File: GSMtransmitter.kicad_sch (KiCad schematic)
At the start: 44 parts, among them J1 Conn_01x06_Pin, J2 Conn_02x02_2.54, J3 Conn_01x05, SW1 SM5-180UP-1, U1 STM32L052C8Tx, Y1 4 MHz, Y2 32768 kHz

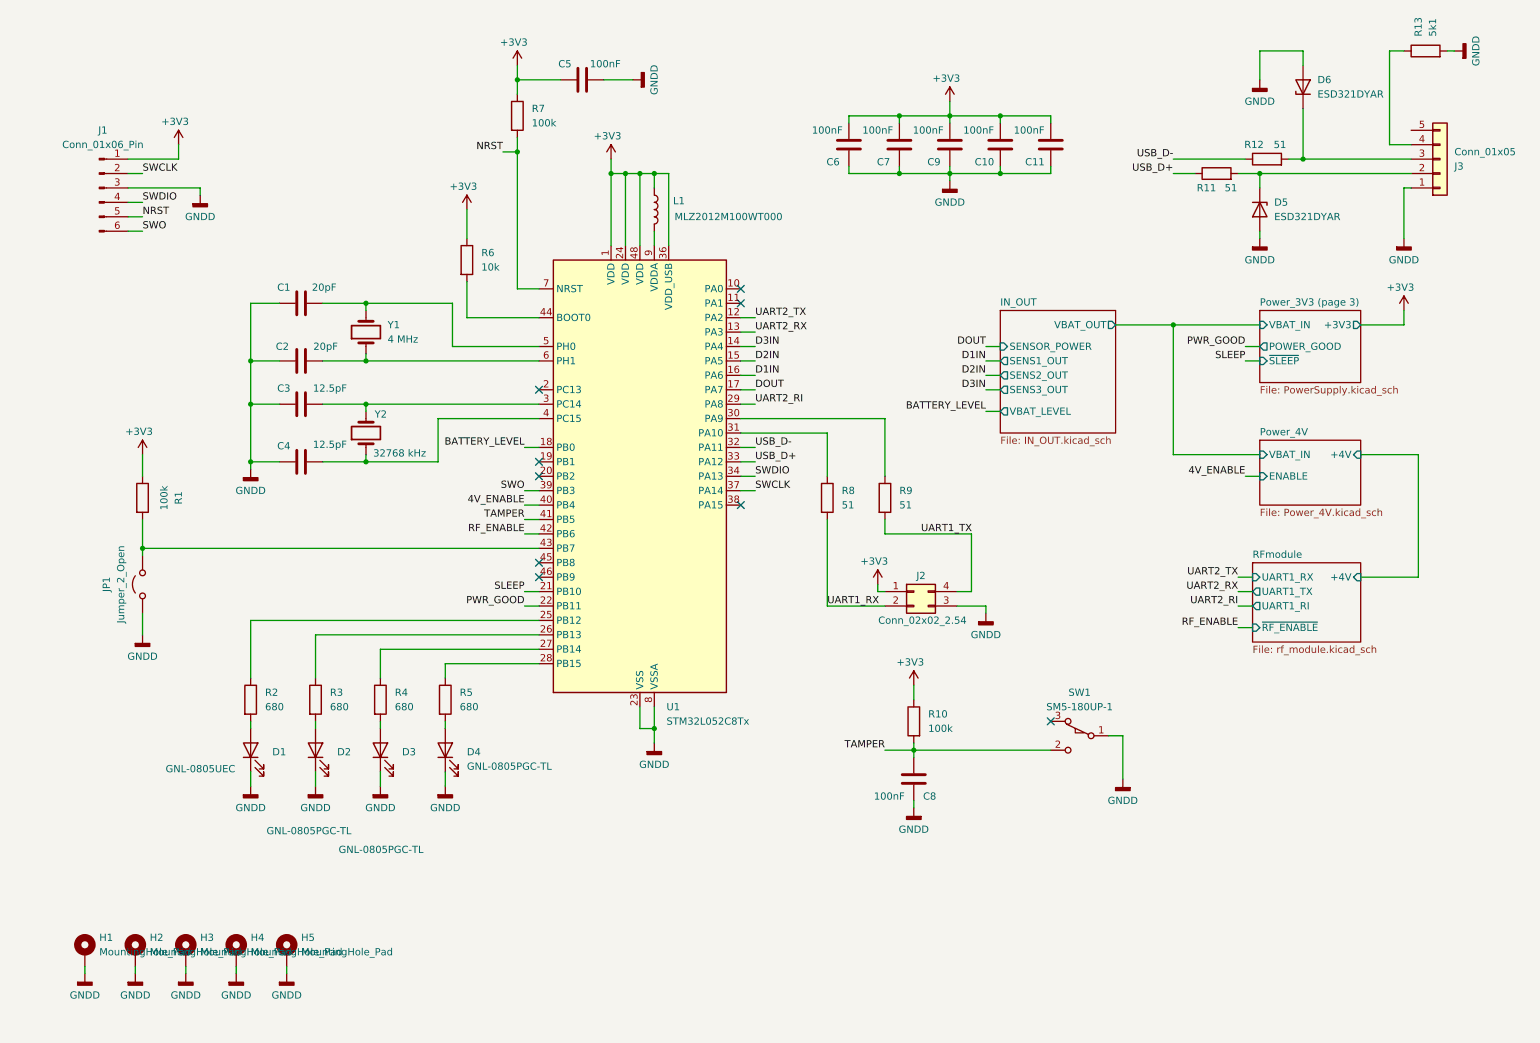
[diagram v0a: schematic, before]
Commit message: Dual SIM version
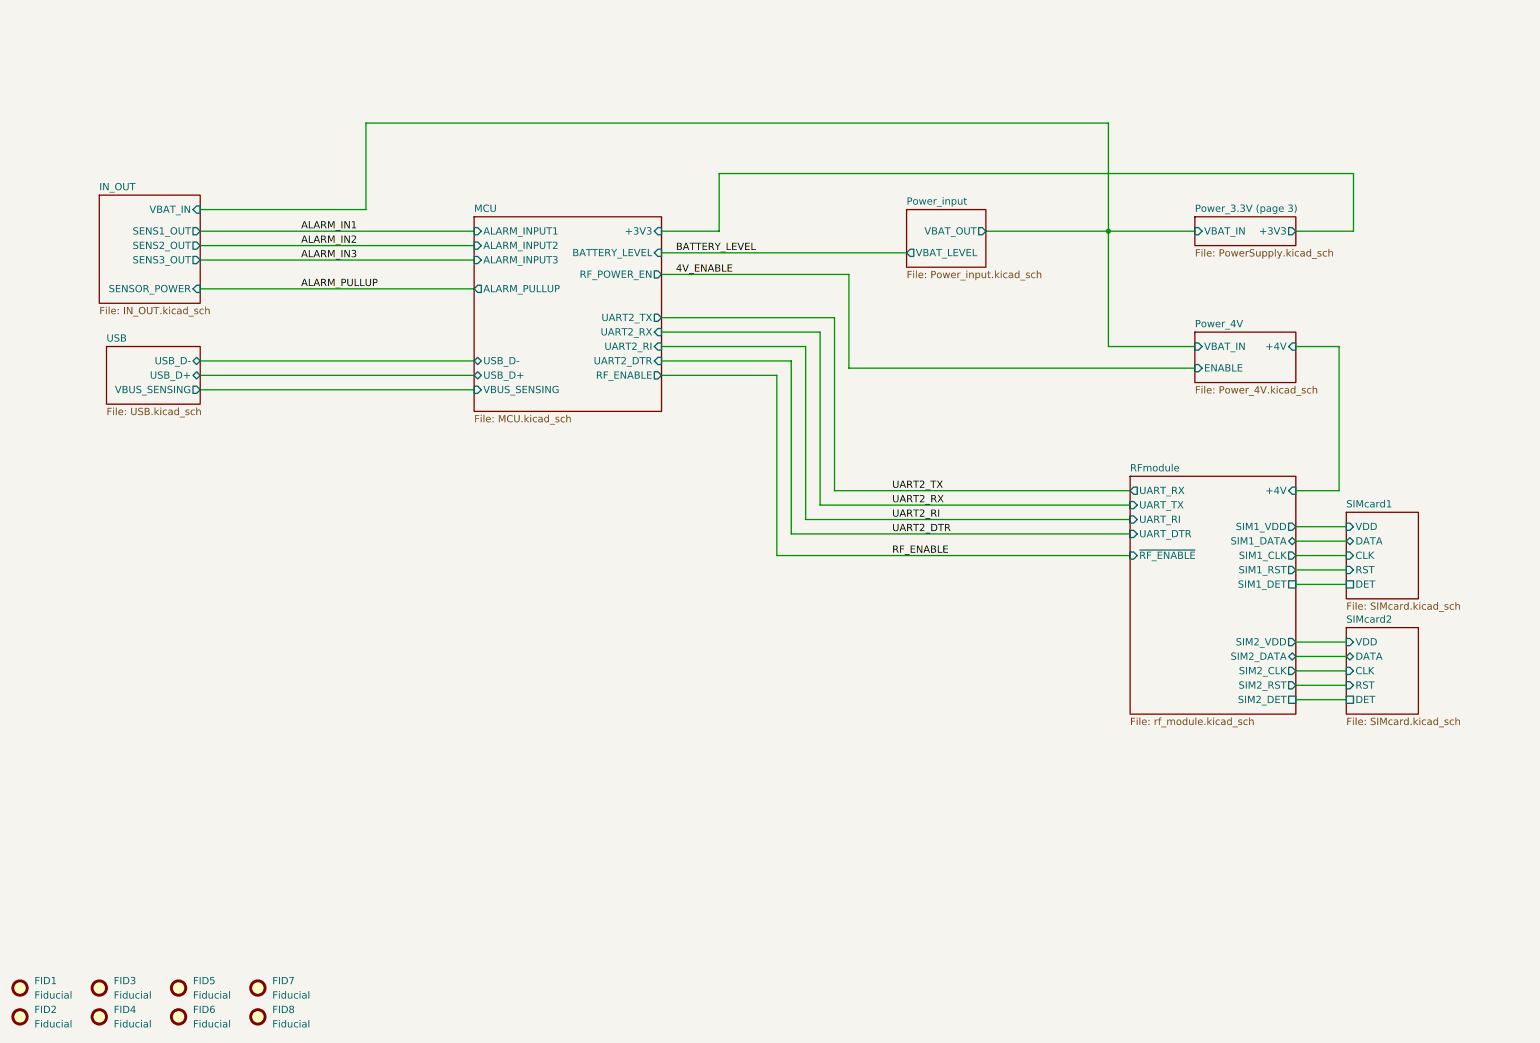
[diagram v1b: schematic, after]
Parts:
- removed C1, C2: 20pF, Capacitor_SMD:C_0805_2012Metric_Pad1.18x1.45mm_HandSolder, symbol Device:C
- removed C10, C11, C5, C6, C7, C8, C9: 100nF, Capacitor_SMD:C_0805_2012Metric_Pad1.18x1.45mm_HandSolder, symbol Device:C
- removed C3, C4: 12.5pF, Capacitor_SMD:C_0805_2012Metric_Pad1.18x1.45mm_HandSolder, symbol Device:C
- removed D1: GNL-0805UEC, LED_SMD:LED_0805_2012Metric_Pad1.15x1.40mm_HandSolder, symbol Device:LED
- removed D2, D3, D4: GNL-0805PGC-TL, LED_SMD:LED_0805_2012Metric_Pad1.15x1.40mm_HandSolder, symbol Device:LED
- removed D5, D6: ESD321DYAR, Diode_SMD:D_SOD-523, symbol Diode:ESD5Zxx
- removed H1, H2, H3, H4: MountingHole_Pad, MountingHole:MountingHole_4.3mm_M4_DIN965_Pad, symbol Mechanical:MountingHole_Pad
- removed H5: MountingHole_Pad, MountingHole:MountingHole_3.5mm_Pad_TopBottom, symbol Mechanical:MountingHole_Pad
- removed J1: Conn_01x06_Pin, Connector_PinHeader_2.54mm:PinHeader_1x06_P2.54mm_Vertical, symbol Connector:Conn_01x06_Pin
- removed J2: Conn_02x02_2.54, Connector_PinSocket_2.54mm:PinSocket_2x02_P2.54mm_Vertical, symbol Connector_Generic:Conn_02x02_Counter_Clockwise
- removed J3: Conn_01x05, Connector_JST:JST_PH_B5B-PH-K_1x05_P2.00mm_Vertical, symbol Connector_Generic:Conn_01x05
- removed JP1: Jumper_2_Open, TestPoint:TestPoint_2Pads_Pitch2.54mm_Drill0.8mm, symbol Jumper:Jumper_2_Open
- removed L1: MLZ2012M100WT000, Inductor_SMD:L_0805_2012Metric_Pad1.05x1.20mm_HandSolder, symbol Device:L
- removed R1, R10, R7: 100k, Resistor_SMD:R_0805_2012Metric_Pad1.20x1.40mm_HandSolder, symbol Device:R
- removed R11, R12, R8, R9: 51, Resistor_SMD:R_0805_2012Metric_Pad1.20x1.40mm_HandSolder, symbol Device:R
- removed R13: 5k1, Resistor_SMD:R_0805_2012Metric_Pad1.20x1.40mm_HandSolder, symbol Device:R
- removed R2, R3, R4, R5: 680, Resistor_SMD:R_0805_2012Metric_Pad1.20x1.40mm_HandSolder, symbol Device:R
- removed R6: 10k, Resistor_SMD:R_0805_2012Metric_Pad1.20x1.40mm_HandSolder, symbol Device:R
- removed SW1: SM5-180UP-1, footprints:SW_XKB_SM5-180UP-1, symbol symbols:SW_SPDT_XKB_SMx-xxxx-1
- removed U1: STM32L052C8Tx, Package_QFP:LQFP-48_7x7mm_P0.5mm, symbol MCU_ST_STM32L0:STM32L052C8Tx
- removed Y1: 4 MHz, Crystal:Crystal_HC49-4H_Vertical, symbol Device:Crystal
- removed Y2: 32768 kHz, Crystal:Crystal_SMD_EuroQuartz_EQ161-2Pin_3.2x1.5mm_HandSoldering, symbol Device:Crystal
- added FID1, FID2, FID3, FID4, FID5, FID6, FID7, FID8: Fiducial, Fiducial:Fiducial_1mm_Mask2mm, symbol Mechanical:Fiducial
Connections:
- no-connect marks 9 -> 0
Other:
- sheet Power_3V3 (page 3) renamed Power_3.3V (page 3)
- added sheet MCU (MCU.kicad_sch)
- added sheet Power_input (Power_input.kicad_sch)
- added sheet SIMcard1 (SIMcard.kicad_sch)
- added sheet SIMcard2 (SIMcard.kicad_sch)
- added sheet USB (USB.kicad_sch)
- sheet IN_OUT ports: added VBAT_IN; removed VBAT_LEVEL, VBAT_OUT
- sheet Power_3.3V (page 3) ports: added none; removed POWER_GOOD, ~{SLEEP}
- sheet RFmodule ports: added SIM1_CLK, SIM1_DATA, SIM1_DET, SIM1_RST, SIM1_VDD, SIM2_CLK, SIM2_DATA, SIM2_DET, SIM2_RST, SIM2_VDD, UART_DTR, UART_RI, UART_RX, UART_TX; removed UART1_RI, UART1_RX, UART1_TX

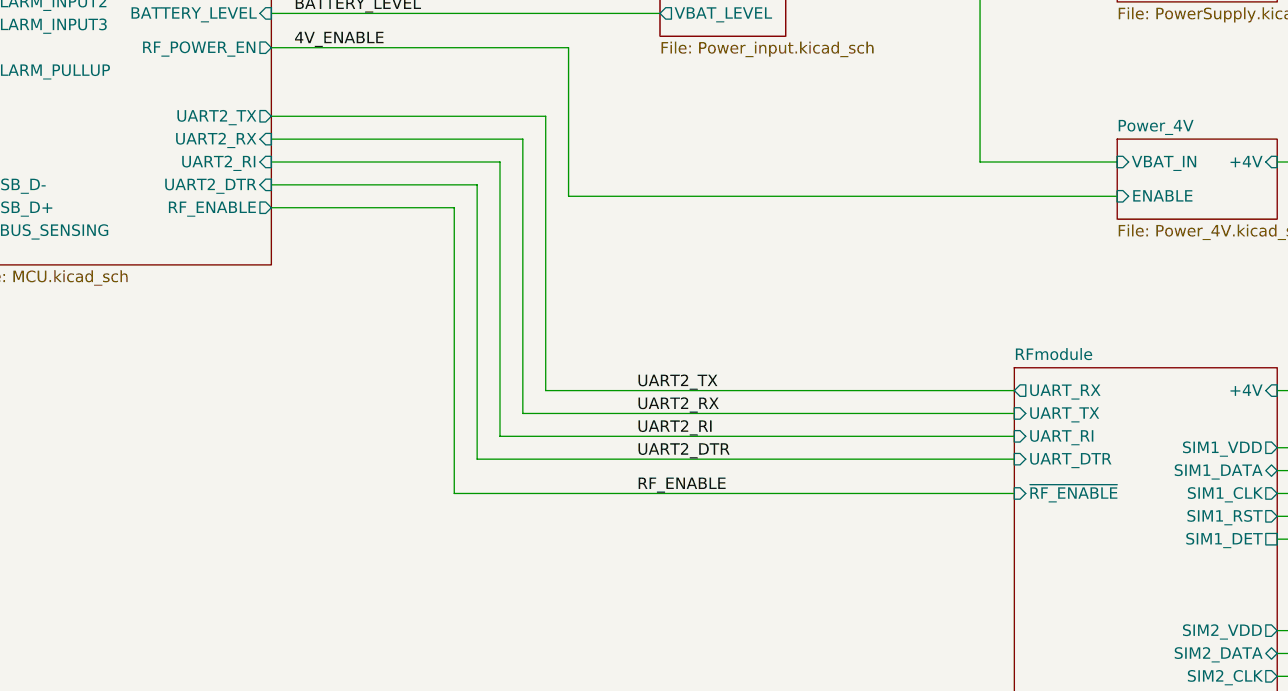
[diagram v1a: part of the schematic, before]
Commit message: Replace SIM800DC with A7682E
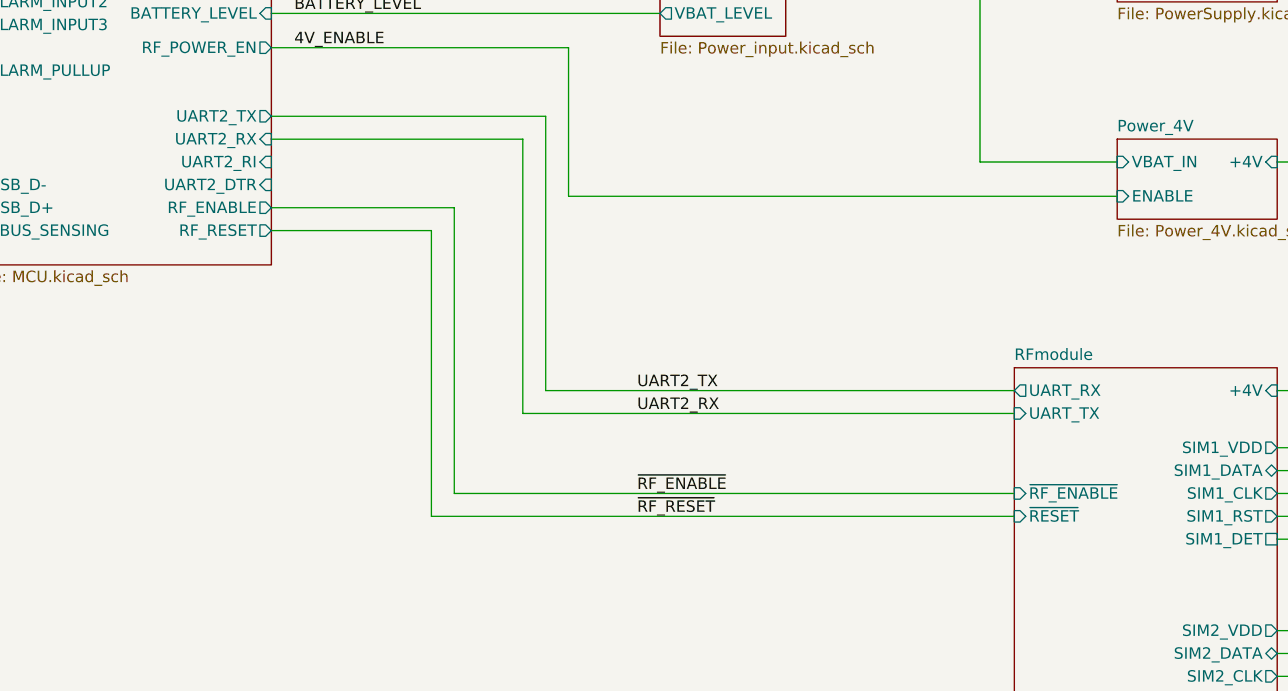
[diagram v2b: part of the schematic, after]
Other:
- sheet MCU ports: added RF_RESET; removed none
- sheet RFmodule ports: added ~{RESET}; removed UART_DTR, UART_RI
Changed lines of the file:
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@@
+	(wire
+		(pts
+			(xy 148.59 81.28) (xy 148.59 113.03)
+		)
+		(stroke
+			(width 0)
+			(type default)
+		)
+	)
 	(wire
 		(pts
@@
 	(wire
 		(pts
-			(xy 156.21 73.66) (xy 156.21 104.14)
-		)
-		(stroke
-			(width 0)
-			(type default)
-		)
-	)
-	(wire
-		(pts
 			(xy 49.53 55.88) (xy 97.79 55.88)
 		)
@@
 	(wire
 		(pts
+			(xy 148.59 113.03) (xy 213.36 113.03)
+		)
+		(stroke
+			(width 0)
+			(type default)
+		)
+	)
+	(wire
+		(pts
 			(xy 49.53 81.28) (xy 97.79 81.28)
 		)
@@
 	(wire
 		(pts
-			(xy 153.67 106.68) (xy 213.36 106.68)
-		)
-		(stroke
-			(width 0)
-			(type default)
-		)
-	)
-	(wire
-		(pts
 			(xy 224.79 73.66) (xy 209.55 73.66)
 		)
@@
 	(wire
 		(pts
-			(xy 130.81 73.66) (xy 156.21 73.66)
-		)
-		(stroke
-			(width 0)
-			(type default)
-		)
-	)
-	(wire
-		(pts
 			(xy 140.97 43.18) (xy 140.97 53.34)
 		)
@@
 	(wire
 		(pts
-			(xy 156.21 104.14) (xy 213.36 104.14)
-		)
-		(stroke
-			(width 0)
-			(type default)
-		)
-	)
-	(wire
-		(pts
 			(xy 161.29 68.58) (xy 161.29 99.06)
 		)
@@
 	(wire
 		(pts
-			(xy 153.67 76.2) (xy 153.67 106.68)
-		)
-		(stroke
-			(width 0)
-			(type default)
-		)
-	)
-	(wire
-		(pts
 			(xy 151.13 78.74) (xy 151.13 110.49)
 		)
@@
 	(wire
 		(pts
-			(xy 130.81 76.2) (xy 153.67 76.2)
-		)
-		(stroke
-			(width 0)
-			(type default)
-		)
-	)
-	(wire
-		(pts
 			(xy 251.46 115.57) (xy 242.57 115.57)
 		)
@@
 		(pts
 			(xy 163.83 60.96) (xy 163.83 77.47)
+		)
+		(stroke
+			(width 0)
+			(type default)
+		)
+	)
+	(wire
+		(pts
+			(xy 130.81 81.28) (xy 148.59 81.28)
 		)
 		(stroke
@@
 		)
 	)
+	(label "~{RF_RESET}"
+		(at 171.45 113.03 0)
+		(effects
+			(font
+				(size 1.27 1.27)
+			)
+			(justify left bottom)
+		)
+	)
 	(label "ALARM_IN2"
 		(at 67.31 55.88 0)
@@
 		)
 	)
-	(label "RF_ENABLE"
+	(label "~{RF_ENABLE}"
 		(at 171.45 110.49 0)
-		(effects
-			(font
-				(size 1.27 1.27)
-			)
-			(justify left bottom)
-		)
-	)
-	(label "UART2_DTR"
-		(at 171.45 106.68 0)
-		(effects
-			(font
-				(size 1.27 1.27)
-			)
-			(justify left bottom)
-		)
-	)
-	(label "UART2_RI"
-		(at 171.45 104.14 0)
 		(effects
 			(font
@@
 			)
 		)
-		(pin "UART_DTR" input
-			(at 213.36 106.68 180)
-			(effects
-				(font
-					(size 1.27 1.27)
-				)
-				(justify left)
-			)
-		)
 		(pin "SIM1_CLK" output
 			(at 242.57 110.49 0)
@@
 			)
 		)
-		(pin "UART_RI" input
-			(at 213.36 104.14 180)
-			(effects
-				(font
-					(size 1.27 1.27)
-				)
-				(justify left)
-			)
-		)
 		(pin "UART_RX" output
 			(at 213.36 99.06 180)
@@
 		(pin "UART_TX" input
 			(at 213.36 101.6 180)
+			(effects
+				(font
+					(size 1.27 1.27)
+				)
+				(justify left)
+			)
+		)
+		(pin "~{RESET}" input
+			(at 213.36 113.03 180)
 			(effects
 				(font
@@
 			)
 		)
+		(pin "RF_RESET" output
+			(at 130.81 81.28 0)
+			(effects
+				(font
+					(size 1.27 1.27)
+				)
+				(justify right)
+			)
+		)
